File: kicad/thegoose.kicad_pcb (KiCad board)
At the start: 4 copper layers, 91 x 47 mm, 182 parts, among them J1 USB_C_Receptacle_USB2.0_16P, J10 IO6, J11 Balance, J12 LED stick, J2 NTC bead 10k B3435, J3 XT60-F pigtail 14AWG, J4 USB-A host, J5 IO1, J6 IO2, J7 IO3, J8 IO4, J9 IO5, Q1 AO4407A, Q2 80N03F, Q3 80N03F, SW1 Power, SW2 BOOT, SW3 RESET, U1 DRV8848, U10 RP2354A, U11 SRV05-4, U12 SY6280AAC, U13 BQ7791501, U14 74AHCT1G125, U2 DRV8848, U3 DRV8848, U4 AP64500SP-13, U5 CH224A, U6 SRV05-4, U7 BQ25798, U8 HT7550-1, U9 XC6206P332MR, Y1 12MHz

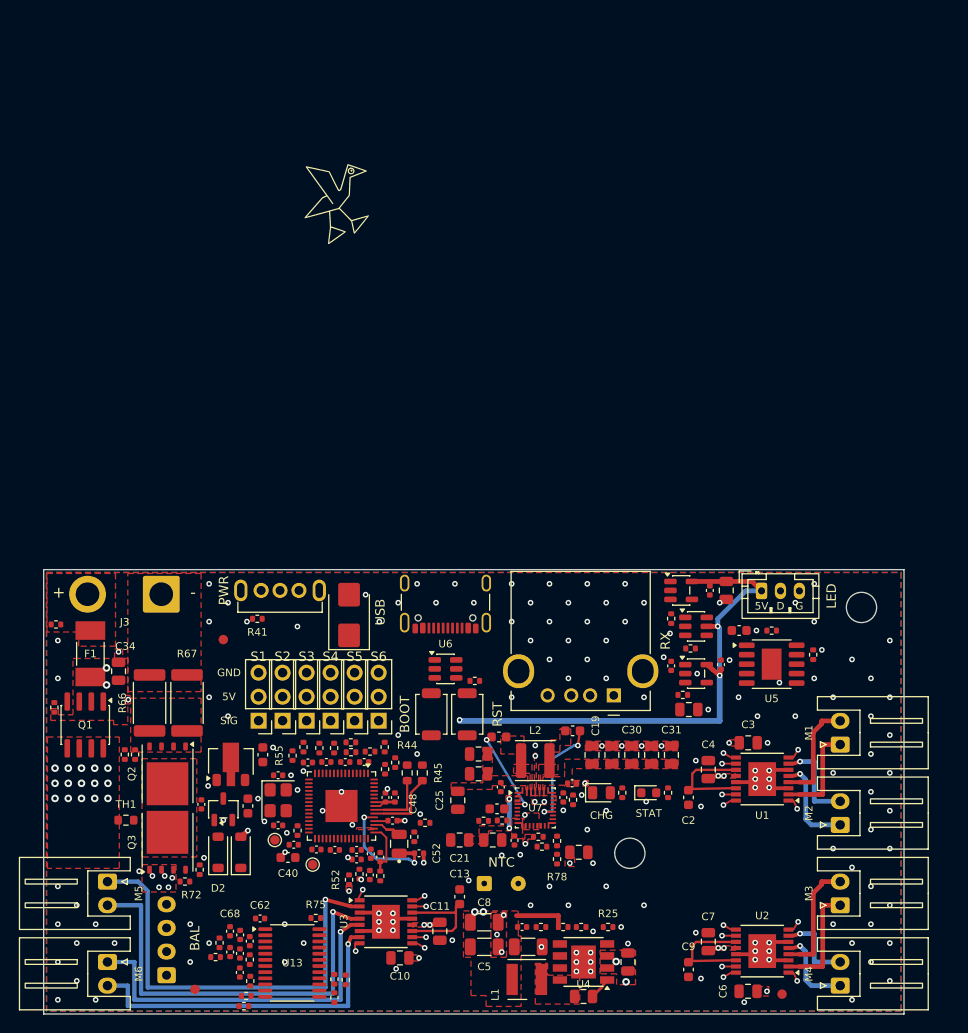
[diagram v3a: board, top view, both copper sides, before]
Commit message: Re-lay out rev 2 around an Ovonic 450 pack on top of the board
The internal pack is now an Ovonic 3S 450 mAh XT30 pack sitting 2 mm
above the board over the low-power logic area, on an XT30 pigtail. The
board is 88.5 x 47 mm with 2 mm corner radii, for a box of about
93.5 x 52 x 24.6 mm whose face has no openings.

- IO S1-S6 are a 3 x 6 right-angle header out of the left end, beside
  M5/M6, replacing the recessed vertical block.
- BOOT is a side-push switch on the top edge behind a pinhole sized for
  a 2.5 mm hex key; RESET is removed, with RUN on a bottom test pad
  beside SWCLK/SWDIO/GND.
- The CHG LED is a side-view part on the top edge; the GPIO status LED
  is removed now that the WS2812B stick shows status.
- The pack NTC is removed (a fixed 10k holds the charger's TS at 25 C);
  the protector's on-board TH1 stays.
- Q1, F1 and the other warm parts moved out from under the pack, and the
  GPIO map was re-swapped for the new placement (I2C on I2C1).

Schematic review passes; PCB review passes every gate except unrouted.

Co-Authored-By: Claude Opus 5.5 <noreply@anthropic.com>
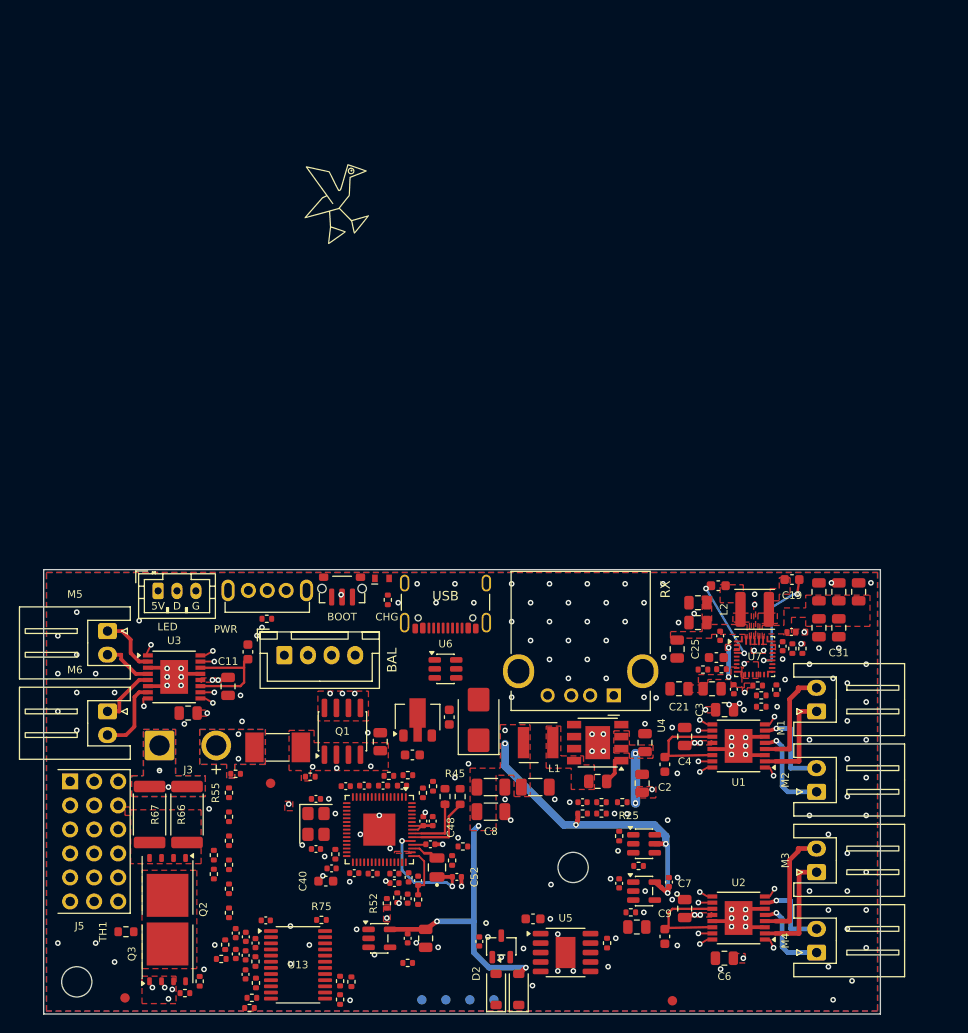
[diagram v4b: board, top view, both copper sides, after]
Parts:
- removed J10: IO6, Connector_PinHeader_2.54mm:PinHeader_1x03_P2.54mm_Vertical
- removed J2: NTC bead 10k B3435, Connector_Wire:SolderWire-0.1sqmm_1x02_P3.6mm_D0.4mm_OD1mm
- removed J6: IO2, Connector_PinHeader_2.54mm:PinHeader_1x03_P2.54mm_Vertical
- removed J7: IO3, Connector_PinHeader_2.54mm:PinHeader_1x03_P2.54mm_Vertical
- removed J8: IO4, Connector_PinHeader_2.54mm:PinHeader_1x03_P2.54mm_Vertical
- removed J9: IO5, Connector_PinHeader_2.54mm:PinHeader_1x03_P2.54mm_Vertical
- removed LED2: red, LED_SMD:LED_0603_1608Metric
- removed R47, R51: 1k, Resistor_SMD:R_0402_1005Metric
- removed SW3: RESET, Button_Switch_SMD:SW_SPST_TS-1088-xR020
- added R81: 10k, Resistor_SMD:R_0402_1005Metric, F.Cu at (180.2, 108.3)
- added TP3: RUN, TestPoint:TestPoint_Pad_D1.0mm, B.Cu at (145.1, 145.5)
- added TP4: GND, TestPoint:TestPoint_Pad_D1.0mm, B.Cu at (147.6, 145.5)
- J11: moved to F.Cu
- J3: value XT60-F pigtail 14AWG -> XT30 pigtail 16AWG; footprint Connector_Wire:SolderWire-2sqmm_1x02_P7.8mm_D2mm_OD3.9mm -> Connector_Wire:SolderWire-1.5sqmm_1x02_P6mm_D1.7mm_OD3mm
- J5: value IO1 -> IO 3x6 RA; footprint Connector_PinHeader_2.54mm:PinHeader_1x03_P2.54mm_Vertical -> hexy:PinHeader_3x06_P2.54mm_Horizontal_WingTAT
- LED1: footprint LED_SMD:LED_0805_2012Metric -> hexy:LED_Everlight_27-21_SideView
- SW2: footprint Button_Switch_SMD:SW_SPST_TS-1088-xR020 -> hexy:SW_Push_1P1T-MP_NO_Horizontal_Alps_SKRTLAE010_JLC
- TP1, TP2: moved to B.Cu
- moved J12 63.8 mm to (112.1, 102.2)
- moved REF** 60.1 mm to (103.5, 143.6)
- moved R80 52.1 mm to (138.5, 141.6)
- moved C69 48.7 mm to (138.5, 139.0)
- moved U14 48.7 mm to (135.5, 139.0)
- moved C70 48.6 mm to (140.4, 139.0)
- moved REF** 41.1 mm to (156.0, 131.5)
- moved C17 37.5 mm to (151.8, 136.9)
- moved U5 37.5 mm to (155.2, 140.5)
- moved R29 37.5 mm to (159.6, 139.5)
- moved J11 36.1 mm to (125.5, 109.0), turned to 0 degrees
- moved C11 34.2 mm to (119.5, 112.3)
- moved C10 34.2 mm to (115.3, 115.2)
- moved C13 34.2 mm to (121.6, 108.7)
- moved U3 34.2 mm to (113.8, 111.3)
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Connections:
- J5 pad 1: Net-(J5-Pin_1) -> GND
- J5 pad 3: GND -> Net-(J5A-SIG)
- R55 pad 2: Net-(J5-Pin_1) -> Net-(J5A-SIG)
- R56 pad 2: Net-(J6-Pin_1) -> Net-(J5B-SIG)
- R57 pad 2: Net-(J7-Pin_1) -> Net-(J5C-SIG)
- R58 pad 2: Net-(J8-Pin_1) -> Net-(J5D-SIG)
- R59 pad 2: Net-(J9-Pin_1) -> Net-(J5E-SIG)
- R60 pad 2: Net-(J10-Pin_1) -> Net-(J5F-SIG)
- U1 pad 10: GPIO0_M2B -> GPIO6_M2B
- U1 pad 15: GPIO11_M1B -> GPIO5_M1B
- U1 pad 16: GPIO10_M1A -> GPIO4_M1A
- U1 pad 9: GPIO1_M2A -> GPIO7_M2A
- U10 pad 10: IO4_GPIO -> GPIO7_M2A
- U10 pad 13: I2C_SCL -> CHG_INT
- U10 pad 14: GPIO10_M1A -> GPIO10_M5A
- U10 pad 15: GPIO11_M1B -> GPIO11_M5B
- U10 pad 16: IO2_GPIO -> GPIO12_M6B
- U10 pad 17: IO1_GPIO -> GPIO13_M6A
- U10 pad 18: IO3_GPIO -> GPIO14_M4A
- U10 pad 19: DRV_FAULT -> GPIO15_M4B
- U10 pad 2: GPIO0_M2B -> GPIO0_M3A
- U10 pad 26: Net-(U10-RUN) -> /MCU & USB/RUN
- U10 pad 27: /MCU & USB/USBA_VBUS_EN -> IO4_GPIO
- U10 pad 28: DRV_SLEEP -> I2C_SCL
- U10 pad 29: GPIO18_M3A -> LED_DIN
- U10 pad 3: GPIO1_M2A -> GPIO1_M3B
- U10 pad 31: GPIO19_M3B -> DRV_FAULT
- U10 pad 32: Net-(U10-GPIO20) -> unconnected-(U10-GPIO20-Pad32)
- U10 pad 33: LED_DIN -> IO1_GPIO
- U10 pad 34: GPIO22_M6B -> IO3_GPIO
- U10 pad 35: GPIO23_M6A -> DRV_SLEEP
- U10 pad 36: GPIO24_M5A -> IO2_GPIO
- U10 pad 37: GPIO25_M5B -> /MCU & USB/USBA_VBUS_EN
- U10 pad 40: /MCU & USB/BAT_SENSE -> IO5_GPIO
- U10 pad 42: IO5_GPIO -> /MCU & USB/BAT_SENSE
- U10 pad 7: GPIO4_M4B -> GPIO4_M1A
- U10 pad 8: GPIO5_M4A -> GPIO5_M1B
- U10 pad 9: CHG_INT -> GPIO6_M2B
- U2 pad 10: GPIO4_M4B -> GPIO15_M4B
- U2 pad 15: GPIO19_M3B -> GPIO1_M3B
- U2 pad 16: GPIO18_M3A -> GPIO0_M3A
- U2 pad 9: GPIO5_M4A -> GPIO14_M4A
- U3 pad 10: GPIO22_M6B -> GPIO12_M6B
- U3 pad 15: GPIO25_M5B -> GPIO11_M5B
- U3 pad 16: GPIO24_M5A -> GPIO10_M5A
- U3 pad 9: GPIO23_M6A -> GPIO13_M6A
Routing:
- net Net-(M5-OUT1): track 45.2 -> 6.45 mm, vias 1 -> 0
- net Net-(M5-OUT2): track 43.3 -> 5.40 mm, vias 1 -> 0
- net Net-(M6-OUT1): track 36.6 -> 6.38 mm, vias 1 -> 0
- net Net-(M6-OUT2): track 34.3 -> 7.99 mm, vias 1 -> 0
- net VSYS: track 0.00 -> 5.25 mm, vias 27 -> 15
- net GPIO12_M6B: track 0.00 -> 0.95 mm, vias 0 -> 1
- net GPIO11_M5B: track 0.00 -> 0.95 mm, vias 0 -> 1
- net GPIO6_M2B: track 0.00 -> 0.95 mm, vias 0 -> 1
- net GPIO5_M1B: track 0.00 -> 0.95 mm, vias 0 -> 1
- net GPIO4_M4B: track 0.95 -> 0.00 mm, vias 1 -> 0
- net GPIO25_M5B: track 0.95 -> 0.00 mm, vias 1 -> 0
- net GPIO22_M6B: track 0.95 -> 0.00 mm, vias 1 -> 0
- net GPIO1_M3B: track 0.00 -> 0.95 mm, vias 0 -> 1
- net GPIO19_M3B: track 0.95 -> 0.00 mm, vias 1 -> 0
- net GPIO15_M4B: track 0.00 -> 0.95 mm, vias 0 -> 1
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- added copper zone on B.Cu, net /Power & charging/BAT_N
- added copper zone on B.Cu, net /Power & charging/PACK+
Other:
- board size 91 x 47 mm -> 88.5 x 47 mm
- board text added: "BOOT: side push SW2, actuator centre 1.7 mm above the board, flush with the top edge at board x 31.61; case pinhole 3.0-3.2 mm"
- board text added: "CHG LED1: side view, lens 0.2 mm behind the top edge at board x 35.83, centre about 0.3 mm above the board; wall hole 1.5 mm"
- board text added: "J5 IO S1 (top) ... S6 (bottom), pins out of the left wall; per port GND (row at the wall, lowest pin) / 5V / SIG (top pin)"
- board text added: "LED STICK ZONE 51 x 10 mm on the inside of the top wall (z about 8-18 mm, above the USB ports): keep the pack clear"
- board text added: "PACK: Ovonic 80C 3S 450 mAh, envelope 52 x 26 x 15 mm (listed 50.5 x 25 x 14)"
- board text added: "SWD / RUN / GND pads TP1-TP4 (bottom): SWCLK, SWDIO, RUN, GND at 2.54 mm"
- board text added: "XT30 MATED PAIR (about 22-31 x 10.2 x 5.2): on edge over the shunts/FETs, into the wall gap at the bottom"
- board text added: "XT30 MATED PAIR (about 31 x 10 x 5.2): flat over the shunts/FETs, or on edge; into the wall gap at the bottom"
- board text added: "XT30 PIGTAIL"
- board text added: "mounting hole under the pack: low-profile or nylon wafer head (< 1.5 mm)"
- board text added: "mounting hole under the pack: low-profile or nylon wafer head (< 1.5 mm); barrier sheet + foam between pack and board"
- board text added: "on top of the board, 2 mm above it (parts under it <= 1.6 mm); leads exit at the left end"
- board text removed: "GND"
- board text removed: "NTC"
- board text removed: "PACK ENVELOPE 74 x 36 x 20 mm (Gens Ace 3S 1000, nominal 71.5 x 35 x 17), 2 mm behind the board"
- board text removed: "RST"
- board text removed: "S1"
- board text removed: "S2"
- board text removed: "S3"
- board text removed: "S4"
- board text removed: "S5"
- board text removed: "S6"
- board text removed: "SIG"
- board text removed: "STAT"
- board text removed: "XT60 MATED PAIR: STAND ON EDGE HERE"
- board text removed: "XT60 PIGTAIL"
- board text removed: "leads exit at x 117 into the strip: XT60 pigtail + mated plug, balance to J11"

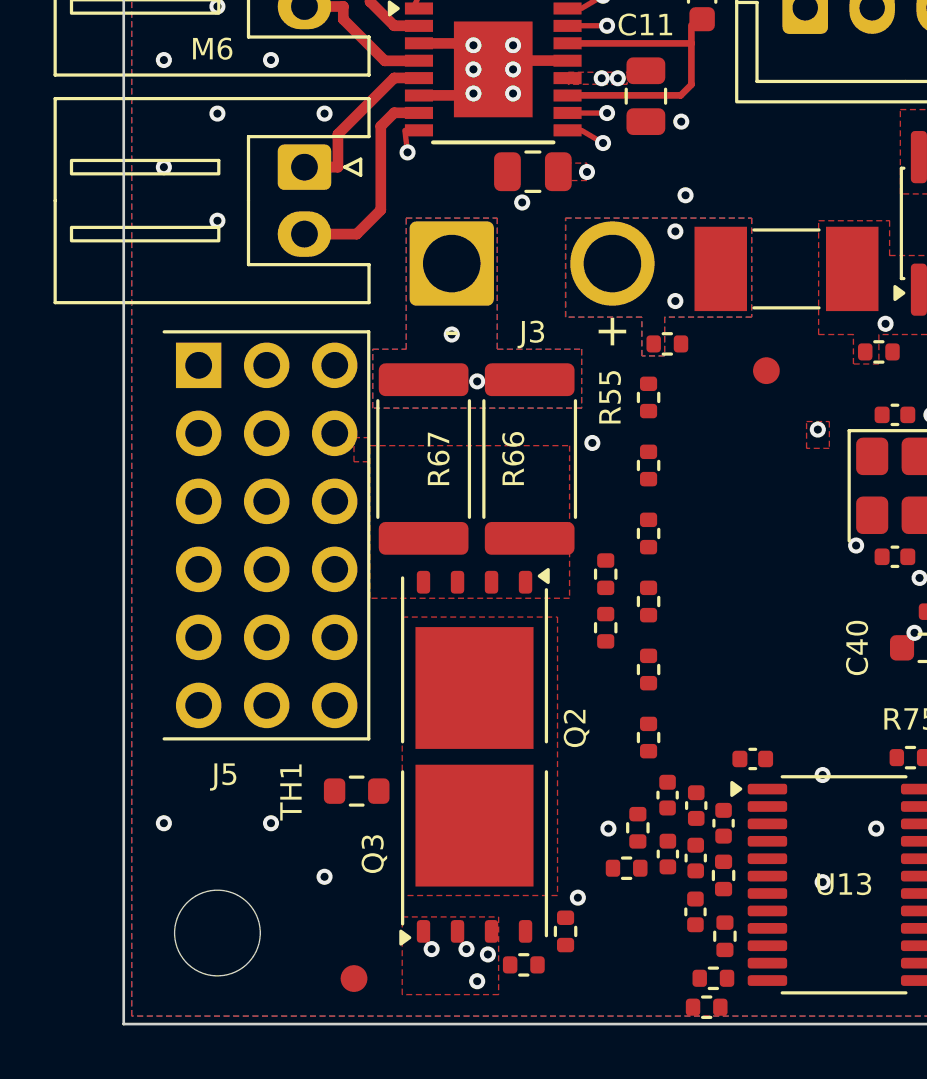
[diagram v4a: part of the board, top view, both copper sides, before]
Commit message: Fit the standard Ovonic 450 pack and recess the IO header
The earlier 50.5 x 25 x 14 mm pack size came from a mislabeled listing.
The layout now uses the standard Ovonic 80C 3S 450 mAh pack (design
envelope 46.5 x 25 x 21 mm) on top of the board, for a box of about
93.5 x 52 x 30 mm; the Long Size pack would have needed a ~110 mm box.

- S1-S6 (J5) move 5.55 mm inboard so the pin tips end 1 mm inside the
  left wall; the FET/shunt strip and nearby passives shift to suit.
- The pack carries a female XT30U-F, so J3 takes a male XT30U-M pigtail
  on 16 AWG. A vertical XT30UPB-M was checked and misses the 1 mm
  clearance under the face.
- IO1-IO4 GPIOs reordered for the new placement.

Schematic review passes; PCB review passes every gate except unrouted.

Co-Authored-By: Claude Opus 5.5 <noreply@anthropic.com>
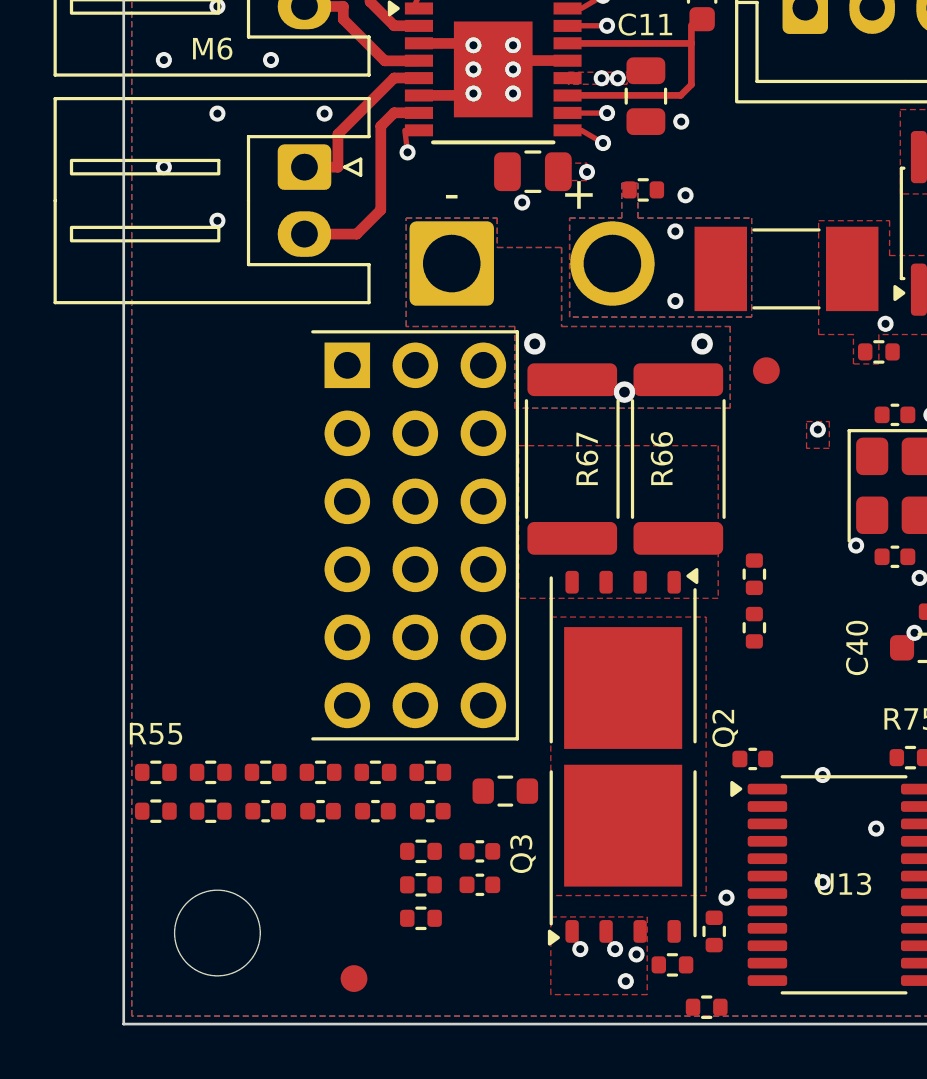
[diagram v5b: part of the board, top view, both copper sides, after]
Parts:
- J3: value XT30 pigtail 16AWG -> XT30U-M pigtail 16AWG
- moved R55 23.1 mm to (101.2, 137.6), turned to 0 degrees
- moved R56 20.0 mm to (103.2, 137.6), turned to 0 degrees
- moved R68 17.7 mm to (101.2, 139.1)
- moved R57 16.9 mm to (105.3, 137.6), turned to 0 degrees
- moved R69 16.0 mm to (103.2, 139.1), turned to 0 degrees
- moved C68 15.0 mm to (105.3, 139.1), turned to 0 degrees
- moved C67 14.0 mm to (107.3, 139.1), turned to 0 degrees
- moved R58 13.8 mm to (107.3, 137.6), turned to 0 degrees
- moved C66 12.1 mm to (109.4, 139.1), turned to 0 degrees
- moved R64 11.5 mm to (111.1, 141.8), turned to 0 degrees
- moved R65 11.3 mm to (111.1, 140.6), turned to 0 degrees
- moved R63 11.1 mm to (111.1, 143.1)
- moved C63 11.0 mm to (111.5, 139.1), turned to 0 degrees
- moved R59 10.9 mm to (109.4, 137.6), turned to 0 degrees
- moved R60 8.25 mm to (111.5, 137.6), turned to 0 degrees
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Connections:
- U10 pad 27: IO4_GPIO -> IO1_GPIO
- U10 pad 33: IO1_GPIO -> IO2_GPIO
- U10 pad 36: IO2_GPIO -> IO4_GPIO
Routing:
- net GND: vias 177 -> 172
- net /Power & charging/BAT_N: vias 2 -> 3
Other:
- board text added: "J5 IO S1 (top) ... S6 (bottom), recessed: pin tips 1 mm inside the left wall's outer face; keep x 0-4.5 clear for the plugs"
- board text added: "PACK: Ovonic 80C 3S 450 mAh (standard), envelope 46.5 x 25 x 21 mm (listed 44.1-46 x 24.2-24.7 x 20.3-20.5)"
- board text added: "XT30 MATED PAIR (about 20 x 10.2 x 5.2 plus leads): on edge over the shunts/FETs, beside the pack's lead end"
- board text added: "XT30U-M PIGTAIL"
- board text added: "on top of the board, 2.4 mm above it (parts under it <= 1.6 mm, barrier + foam between); leads exit at the left end"
- board text removed: "J5 IO S1 (top) ... S6 (bottom), pins out of the left wall; per port GND (row at the wall, lowest pin) / 5V / SIG (top pin)"
- board text removed: "PACK: Ovonic 80C 3S 450 mAh, envelope 52 x 26 x 15 mm (listed 50.5 x 25 x 14)"
- board text removed: "XT30 MATED PAIR (about 22-31 x 10.2 x 5.2): on edge over the shunts/FETs, into the wall gap at the bottom"
- board text removed: "XT30 MATED PAIR (about 31 x 10 x 5.2): flat over the shunts/FETs, or on edge; into the wall gap at the bottom"
- board text removed: "XT30 PIGTAIL"
- board text removed: "mounting hole under the pack: low-profile or nylon wafer head (< 1.5 mm)"
- board text removed: "on top of the board, 2 mm above it (parts under it <= 1.6 mm); leads exit at the left end"
